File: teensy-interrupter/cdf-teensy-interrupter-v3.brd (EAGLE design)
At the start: 76.2 x 80 mm, 42 parts, among them IC1 TP4056, Q1 BC817-40LT1SMD

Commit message: More work
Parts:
- removed MIDI, PULSE: 100SP1T1B4M2QE, keves:100SP1T1B4M2QE
- removed PULSE_DUTY, PULSE_WIDTH: 10K PTV09A-4025F-B103, Bourns:PTV09A-4
- removed SW1: (no value), adafruit:EG1390
- added D1, D3: 1A/23V/620mV, SparkFun-DiscreteSemi:SOD-323
- added PWR: 100SP1T1B4M2QE, keves:100SP1T1B4M2QE
- added R12: 50000, rcl:R0805
- added R13: 100000, rcl:R0805
- added S1: ENCODER-2LED, SparkFun-Switches:ENCODER_LED_2
- R3, R5: value 330 -> 100
- R7: value 68 -> 27
- moved R11 111.0 mm to (57.4, 17.5), turned to 180 degrees
- moved C1 103.7 mm to (57.3, 15.0), turned to 180 degrees
- moved VUSB 103.6 mm to (43.7, 2.67)
- moved CHARGED 101.5 mm to (75.6, 14.7), turned to 90 degrees
- moved CHARGING 95.8 mm to (75.9, 18.2), turned to 90 degrees
- moved R8 85.0 mm to (70.9, 14.6)
- moved R6 84.4 mm to (71.8, 17.9)
- moved B- 73.2 mm to (67.7, 2.41), turned to 90 degrees
- moved B+ 69.3 mm to (64.9, 2.41), turned to 90 degrees
- moved IC1 68.5 mm to (64.3, 16.4)
- moved U$4 58.8 mm to (0.76, 33.9), turned to 90 degrees
- moved FB2 34.2 mm to (19.6, 28.8), turned to 180 degrees
- moved R2 32.6 mm to (19.7, 42.4), turned to 0 degrees
- moved C3 32.6 mm to (19.7, 32.4), turned to 180 degrees
- moved FB1 31.9 mm to (19.7, 39.0), turned to 180 degrees
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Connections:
- net RX renamed MIDI_RX
- removed net PULSE_DUTY: PULSE_DUTY.2, U$1.15/A1
- removed net PULSE_WIDTH: PULSE_WIDTH.2, U$1.14/A0
- removed net TX2: U$1.22/A8
- removed net TX3: U$1.23/A9
- new net ENC_A: S1.A, U$1.14/A0
- new net ENC_B: S1.B, U$1.15/A1
- new net ENC_Z: S1.SW, U$1.16/A2
- new net N$23: B+.1, D3.A, IC1.5
- new net V_SENSE: R12.1, R13.2
- net +3V3: now also R5.2, S1.C, U$3.2; no longer MIDI.P$1, PULSE.P$1, PULSE_DUTY.3, PULSE_WIDTH.3
- net +5V: now also VR1.1; no longer R3.2, R5.2, R7.2, U$3.2, VR1.3
- net GND: now also R13.1, VR1.3; no longer MIDI.P$3, PULSE.P$3, PULSE_DUTY.1, PULSE_WIDTH.1, VR1.1
- net MIDI_MODE: no longer MIDI.P$2
- net N$20: now also D1.C, D3.C, PWR.P$2; no longer B+.1, IC1.5, SW1.O2, SW1.S1
- net N$22: now also D1.A, VUSB.1; no longer SW1.P1
- net N$24: now also R3.2, R7.2; no longer SW1.O1, SW1.S2, VUSB.1
- net PULSE_MODE: no longer PULSE.P$2
- net V+: now also PWR.P$3, R12.2; no longer SW1.P2
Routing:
- net +3V3: track 56.6 -> 0.00 mm
- net MIDI_MODE: track 38.9 -> 0.00 mm, vias 1 -> 0
- net PULSE_MODE: track 35.6 -> 0.00 mm, vias 1 -> 0
- net PULSE_DUTY: track 29.0 -> 0.00 mm
- net PULSE_WIDTH: track 15.3 -> 0.00 mm
- net EMERGENCY: track 49.3 -> 55.8 mm

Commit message: WIP?
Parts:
- removed B+, B-: (no value), adafruit:1X01
- removed EMERGENCY: TL1105LF250Q, SparkFun-Electromechanical:TACTILE-PTH
- removed R4: 220, rcl:0204/7
- removed U$1: TEENSY_3.1_DIL, Teensy_3_and_LC_Series_Boards_v1.1:TEENSY3-DIL
- removed U$3: LCD-HD447804-HOLES16X2-4-HOLES, HD44780LCD:LCD-16X2-4HOLES
- removed U$4: MIDIJACK, adafruit:CP-2350
- removed VR1: 10k, SparkFun-Resistors:TRIMPOT-PTH-3386U
- added BATT, ESTOP: (no value), pinhead:1X02
- added MIDI: MIDIJACK, adafruit:CP-2350
- added R14, R15: 100, rcl:R0805
- added SCRN: (no value), adafruit:1X03
- added TEENSY: TEENSY_3.1_DIL, Teensy_3_and_LC_Series_Boards_v1.1:TEENSY3-DIL
- moved S1 95.0 mm to (61.2, 67.3), turned to 270 degrees
- moved H3 89.8 mm to (90.2, 57.7)
- moved OPT1 76.9 mm to (42.0, 2.16), turned to 180 degrees
- moved R12 76.5 mm to (39.6, 40.1)
- moved R13 74.1 mm to (39.6, 42.7)
- moved LED_TX 69.0 mm to (47.8, 5.71), turned to 180 degrees
- moved R3 56.7 mm to (44.6, 14.9), turned to 180 degrees
- moved R7 56.2 mm to (40.0, 14.9)
- moved C3 47.0 mm to (60.1, 8.38), flipped to the top, turned to 90 degrees
- moved Q1 46.7 mm to (45.0, 18.9), turned to 270 degrees
- moved FB2 46.3 mm to (65.2, 20.8), flipped to the top, turned to 90 degrees
- moved LED_POWER 44.2 mm to (45.7, 67.3)
- moved C2 43.2 mm to (60.1, 20.6), flipped to the top, turned to 90 degrees
- moved R5 43.1 mm to (49.8, 67.3)
- moved FB1 39.8 mm to (55.0, 20.7), flipped to the top, turned to 90 degrees
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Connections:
- removed net +5V: R4.1, VR1.1
- removed net LCD_D4: U$1.5, U$3.11
- removed net LCD_D5: U$1.6, U$3.12
- removed net LCD_D6: U$1.7, U$3.13
- removed net LCD_D7: U$1.8, U$3.14
- removed net LCD_EN: U$1.4, U$3.6
- removed net LCD_RS: U$1.3, U$3.4
- removed net MIDI_MODE: U$1.10
- removed net N$23: B+.1, D3.A, IC1.5
- removed net N$5: U$3.3, VR1.2
- removed net N$6: R4.2, U$3.15
- removed net PULSE_MODE: U$1.9
- new net B+: BATT.2, D3.A, IC1.5
- new net B+1: ESTOP.2
- new net IND_G: R15.1, TEENSY.17/A3
- new net IND_R: R14.1, TEENSY.18/A4
- new net N$25: R15.2, S1.+G
- new net N$26: R14.2, S1.+R
- new net SCRN_TX: SCRN.1, TEENSY.1
- net +3V3: now also SCRN.3, TEENSY.3.3V; no longer U$1.3.3V, U$3.2
- net AGND: now also TEENSY.AGND; no longer U$1.AGND
- net EMERGENCY: now also TEENSY.19/A5; no longer EMERGENCY.1, U$1.11
- net ENC_A: now also TEENSY.15/A1; no longer U$1.14/A0
- net ENC_B: now also TEENSY.14/A0; no longer U$1.15/A1
- net ENC_Z: now also TEENSY.16/A2; no longer U$1.16/A2
- net GND: now also BATT.1, ESTOP.1, SCRN.2, TEENSY.GND; no longer B-.1, EMERGENCY.3, U$1.GND, U$3.1, U$3.16, U$3.5, VR1.3
- net MIDI_RX: now also TEENSY.0; no longer U$1.0
- net N$1: now also MIDI.4; no longer U$4.4
- net N$13: now also MIDI.2; no longer U$4.2
- net N$14: now also MIDI.PE, MIDI.PE1, MIDI.PE2, MIDI.PE@; no longer U$4.PE, U$4.PE1, U$4.PE2, U$4.PE@
- net N$15: now also MIDI.5; no longer U$4.5
- net TX1: now also TEENSY.21/A7; no longer U$1.21/A7
- net V+: now also TEENSY.VIN; no longer U$1.VIN
- net V_SENSE: now also TEENSY.20/A6
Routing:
- net ENC_Z: track 0.00 -> 87.0 mm
- net MIDI_RX: track 0.00 -> 84.0 mm, vias 0 -> 1
- net ENC_A: track 0.00 -> 66.9 mm
- net ENC_B: track 0.00 -> 60.7 mm
- net EMERGENCY: track 55.8 -> 5.46 mm
- net N$26: track 0.00 -> 49.9 mm
- net V+: track 0.00 -> 48.6 mm
- net N$25: track 0.00 -> 42.1 mm
- net N$22: track 0.00 -> 38.3 mm
- net V_SENSE: track 0.00 -> 29.7 mm
- net IND_G: track 0.00 -> 29.5 mm
- net B+: track 0.00 -> 26.2 mm
- net LCD_D4: track 19.0 -> 0.00 mm
- net LCD_D5: track 18.6 -> 0.00 mm
- net LCD_D7: track 18.5 -> 0.00 mm
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- added copper zone on layer 1, net +3V3
- removed copper zone on layer 1, net +5V
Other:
- board size 76.2 x 80 mm -> 75.6 x 80.4 mm
- board text added: "CDF Interrupter v3 2021"
- board text removed: "CDF Interrupter v2 )'( 2017"

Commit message: v3 first press
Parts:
- removed D2: (no value), diode:DO-214AC
- removed LED_TX: (no value), adafruit:CHIP-LED0805
- removed PWR: 100SP1T1B4M2QE, keves:100SP1T1B4M2QE
- added D4: 1A/23V/620mV, SparkFun-DiscreteSemi:SOD-323
- added POWER: (no value), pinhead:1X02
- added TX1: (no value), adafruit:CHIP-LED0805
- H1, H2, H3, H4: value MOUNT-HOLE3.3 -> MOUNT-PAD-ROUND3.0; device holes:3,3 -> holes:3,0-PAD
- moved H3 101.8 mm to (3.81, 3.81), turned to 0 degrees
- moved H1 74.4 mm to (68.6, 3.81), turned to 0 degrees
- moved R5 63.6 mm to (23.7, 9.27), turned to 270 degrees
- moved LED_POWER 58.3 mm to (23.7, 13.3), turned to 0 degrees
- moved BATT 51.2 mm to (12.8, 29.8)
- moved H4 50.7 mm to (3.81, 41.9), turned to 0 degrees
- moved ESTOP 45.4 mm to (12.8, 23.4), turned to 270 degrees
- moved S1 43.1 mm to (40.8, 29.3), turned to 180 degrees
- moved H2 38.4 mm to (68.6, 41.9), turned to 0 degrees
- moved SCRN 33.8 mm to (12.8, 15.6)
- moved R12 33.1 mm to (27.7, 9.27), turned to 270 degrees
- moved R13 31.4 mm to (27.7, 13.6), turned to 270 degrees
- moved VUSB 29.6 mm to (12.8, 35.0), turned to 90 degrees
- moved R14 25.7 mm to (26.7, 22.2), turned to 180 degrees
- moved R15 25.6 mm to (26.7, 24.8), turned to 180 degrees
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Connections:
- net N$24 renamed 3.3V
- removed net B+1: ESTOP.2
- net EMERGENCY: now also ESTOP.2, TEENSY.5; no longer TEENSY.19/A5
- net ENC_A: now also TEENSY.13; no longer TEENSY.15/A1
- net GND: now also H1.B3,0, H2.B3,0, H3.B3,0, H4.B3,0
- net N$10: now also TX1.A; no longer LED_TX.A
- net N$11: now also TX1.C; no longer LED_TX.C
- net N$2: now also D4.C; no longer D2.C
- net N$20: now also POWER.1; no longer PWR.P$2
- net N$3: now also D4.A; no longer D2.A
- net V+: now also POWER.2; no longer PWR.P$3
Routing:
- net ENC_Z: track 87.0 -> 13.7 mm
- net ENC_A: track 66.9 -> 13.1 mm
- net ENC_B: track 60.7 -> 8.58 mm
- net N$26: track 49.9 -> 17.5 mm
- net N$20: track 9.54 -> 41.5 mm
- net N$25: track 42.1 -> 15.6 mm
- net IND_G: track 29.5 -> 4.51 mm
- net V_SENSE: track 29.7 -> 9.16 mm
- net MIDI_RX: track 84.0 -> 64.1 mm, vias 1 -> 0
- net V+: track 48.6 -> 30.7 mm
- net IND_R: track 13.9 -> 4.51 mm
- net SCRN_TX: track 0.00 -> 7.77 mm
- net GND: track 13.9 -> 20.4 mm, vias 8 -> 9
- net N$10: track 9.02 -> 3.72 mm
- net N$3: track 14.3 -> 9.04 mm
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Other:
- board size 75.6 x 80.4 mm -> 72.4 x 45.7 mm
- board text added: "+"
- board text added: "-"

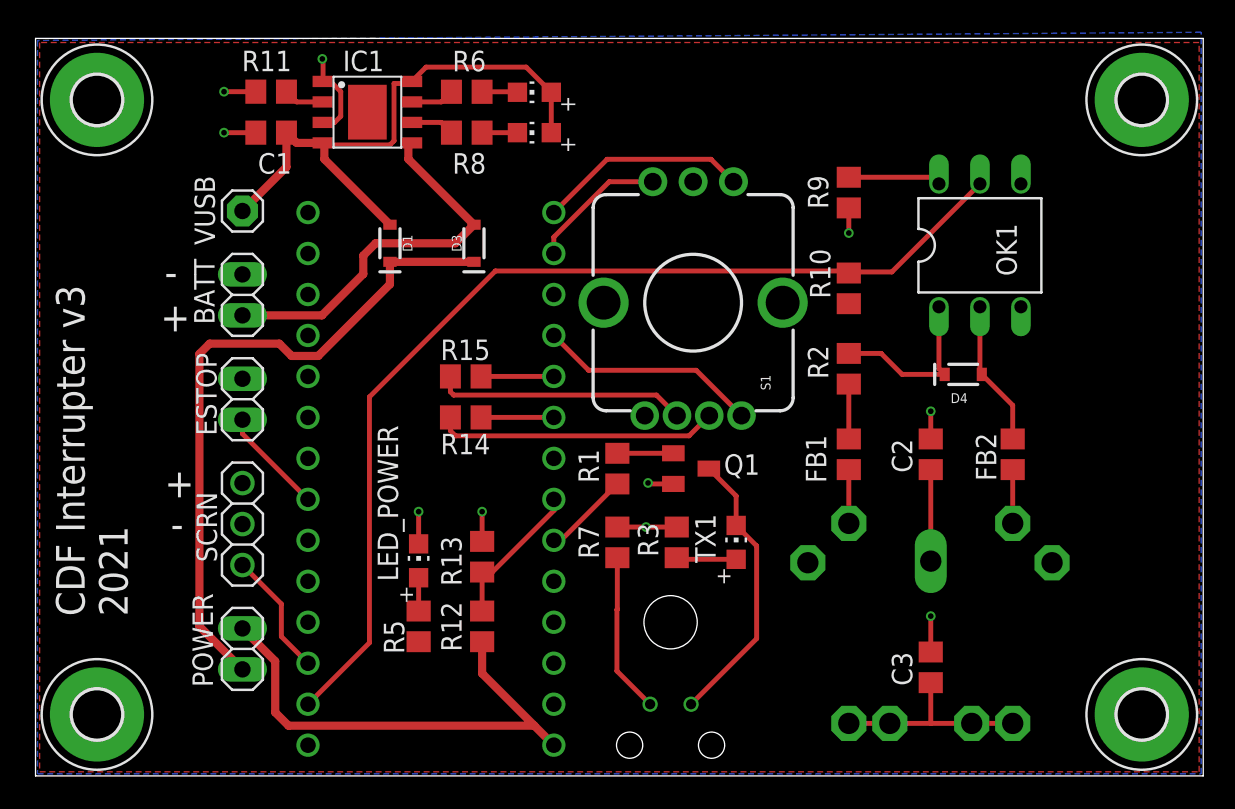
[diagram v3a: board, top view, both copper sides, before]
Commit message: Small board shrink
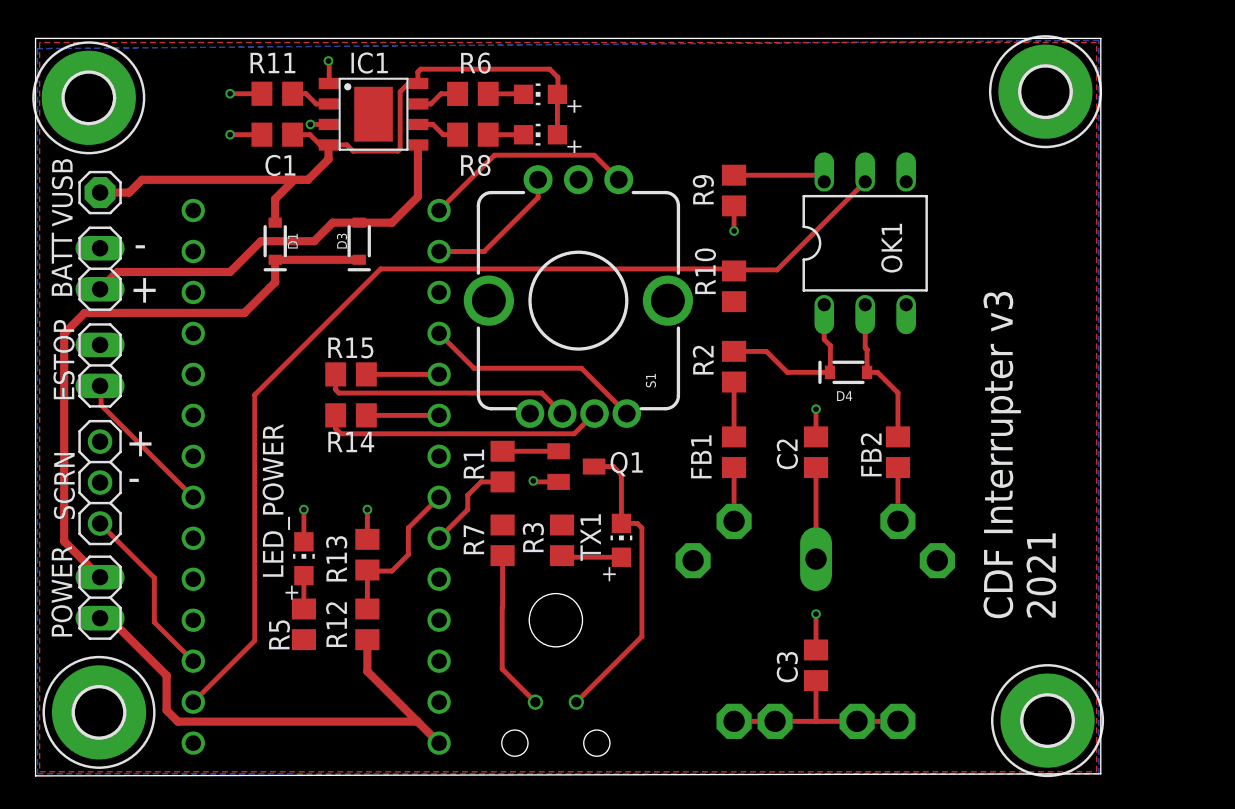
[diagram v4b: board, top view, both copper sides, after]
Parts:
- moved POWER 9.38 mm to (4.00, 11.0), turned to 270 degrees
- moved SCRN 9.19 mm to (4.00, 18.2)
- moved ESTOP 9.07 mm to (4.00, 25.4)
- moved BATT 8.97 mm to (4.00, 31.4)
- moved VUSB 8.90 mm to (4.00, 36.2)
- moved C2 7.11 mm to (48.4, 20.1)
- moved C3 7.11 mm to (48.4, 6.86)
- moved D3 7.11 mm to (20.1, 33.1)
- moved D4 7.11 mm to (50.4, 25.0)
- moved FB2 7.11 mm to (53.5, 20.1)
- moved MIDI 7.11 mm to (48.4, 0.76)
- moved Q1 7.11 mm to (33.5, 19.2)
- moved R14 7.11 mm to (19.6, 22.4)
- moved R15 7.11 mm to (19.6, 24.9)
- moved S1 7.11 mm to (33.7, 29.5)
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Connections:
- removed net 3.3V: R3.2, R7.2
- net +3V3: now also R3.2, R7.2
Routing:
- net N$22: track 36.7 -> 44.3 mm
- net N$20: track 41.5 -> 37.0 mm
- net 3.3V: track 3.68 -> 0.00 mm, vias 1 -> 0
- net SCRN_TX: track 7.77 -> 10.9 mm
- net EMERGENCY: track 6.62 -> 9.30 mm
- net GND: track 20.4 -> 17.9 mm, vias 9 -> 10
- net N$11: track 17.5 -> 18.8 mm
- net V+: track 30.7 -> 31.9 mm
- net B+: track 24.2 -> 25.3 mm
- net V_SENSE: track 9.16 -> 9.75 mm
- net TX1: track 5.38 -> 5.91 mm
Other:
- board size 72.4 x 45.7 mm -> 66 x 45.7 mm

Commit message: As printed
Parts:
- moved H3 0.72 mm to (3.43, 3.43)
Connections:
- net GND: now also S1.GND
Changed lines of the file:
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@@
 <attribute name="POPULARITY" value="17" x="62.611" y="42.418" size="1.778" layer="27" display="off"/>
 </element>
-<element name="H3" library="holes" library_urn="urn:adsk.eagle:library:237" package="3,0-PAD" package3d_urn="urn:adsk.eagle:package:14280/1" value="MOUNT-PAD-ROUND3.0" x="3.937" y="3.937" smashed="yes">
-<attribute name="POPULARITY" value="17" x="3.937" y="3.937" size="1.778" layer="27" display="off"/>
+<element name="H3" library="holes" library_urn="urn:adsk.eagle:library:237" package="3,0-PAD" package3d_urn="urn:adsk.eagle:package:14280/1" value="MOUNT-PAD-ROUND3.0" x="3.429" y="3.429" smashed="yes">
+<attribute name="POPULARITY" value="17" x="3.429" y="3.429" size="1.778" layer="27" display="off"/>
 </element>
 <element name="H4" library="holes" library_urn="urn:adsk.eagle:library:237" package="3,0-PAD" package3d_urn="urn:adsk.eagle:package:14280/1" value="MOUNT-PAD-ROUND3.0" x="3.302" y="42.037" smashed="yes">
@@
 <wire x1="51.435" y1="29.21" x2="51.435" y2="26.543" width="0.3048" layer="1"/>
 <wire x1="51.562" y1="26.416" x2="51.435" y2="26.543" width="0.3048" layer="1"/>
-<wire x1="51.562" y1="25.03095" x2="51.55005" y2="25.019" width="0.3048" layer="1"/>
+<wire x1="51.55005" y1="26.40405" x2="51.562" y2="26.416" width="0.3048" layer="1"/>
 <wire x1="51.55005" y1="25.019" x2="52.197" y2="25.019" width="0.3048" layer="1"/>
 <wire x1="51.55005" y1="25.019" x2="51.55005" y2="26.40405" width="0.3048" layer="1"/>
-<wire x1="51.55005" y1="26.40405" x2="51.562" y2="26.416" width="0.3048" layer="1"/>
 </signal>
 <signal name="GND" airwireshidden="yes">
@@
 <wire x1="18.205" y1="40.386" x2="17.0404" y2="40.386" width="0.3048" layer="1"/>
 <via x="17.0404" y="40.386" extent="1-16" drill="0.35"/>
+<contactref element="S1" pad="GND"/>
 </signal>
 <signal name="N$4">

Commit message: V3r1
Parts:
- removed R14, R15: 100, rcl:R0805
- removed S1: ENCODER-2LED, SparkFun-Switches:ENCODER_LED_2
- added C4: 10uF, rcl:C0805
- added J2, J3: 4p-2.54, OPL_Connector:H4-2.54
- added R16, R17: 100, rcl:R0805
- added R4: 10k, rcl:R0805
- R11: value 1.2K -> 10k
- moved BATT 26.8 mm to (30.6, 35.1), turned to 180 degrees
- moved CHARGING 25.9 mm to (20.8, 18.6), turned to 0 degrees
- moved CHARGED 25.3 mm to (17.7, 18.5), turned to 0 degrees
- moved VUSB 20.7 mm to (3.37, 15.5)
- moved R6 20.5 mm to (20.8, 22.8), turned to 270 degrees
- moved R8 19.5 mm to (17.7, 22.7), turned to 270 degrees
- moved D1 14.5 mm to (13.5, 18.7), turned to 270 degrees
- moved IC1 12.1 mm to (19.6, 29.0), turned to 270 degrees
- moved D3 11.1 mm to (13.5, 24.3)
- moved R11 10.3 mm to (21.8, 34.5)
- moved SCRN 9.24 mm to (3.49, 27.4), turned to 270 degrees
- moved D4 8.77 mm to (57.5, 19.9), turned to 90 degrees
- moved H2 7.64 mm to (62.1, 34.8)
- moved H4 7.27 mm to (3.94, 34.8)
- moved C1 5.54 mm to (16.9, 34.5), turned to 0 degrees
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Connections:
- net N$20 renamed SW
- net N$22 renamed V_USB
- removed net N$25: R15.2, S1.+G
- removed net N$26: R14.2, S1.+R
- new net N$20: J2.3, R16.1
- new net N$5: J3.1, R4.2
- new net N$6: J2.2, R17.1
- net +3V3: now also R4.1; no longer S1.C
- net B+: now also C4.1
- net ENC_A: now also J3.2; no longer S1.A
- net ENC_B: now also J3.3; no longer S1.B
- net ENC_Z: now also J2.1; no longer S1.SW
- net GND: now also C4.2, J2.4; no longer S1.GND
- net IND_G: now also R17.2; no longer R15.1
- net IND_R: now also R16.2; no longer R14.1
- net SCRN_TX: now also TEENSY.10; no longer TEENSY.1
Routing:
- net N$26: track 17.5 -> 0.00 mm
- net SW: track 37.0 -> 20.0 mm, vias 0 -> 1
- net N$25: track 15.6 -> 0.00 mm
- net N$2: track 10.8 -> 23.1 mm
- net ENC_B: track 8.63 -> 16.9 mm
- net B+: track 25.3 -> 33.1 mm
- net MIDI_RX: track 64.1 -> 58.9 mm
- net N$6: track 0.00 -> 4.70 mm
- net SCRN_TX: track 10.9 -> 6.30 mm
- net N$20: track 0.00 -> 4.30 mm
- net V_SENSE: track 9.75 -> 12.7 mm
- net N$5: track 0.00 -> 2.86 mm
- net ENC_A: track 13.2 -> 16.0 mm
- net GND: track 17.9 -> 20.6 mm, vias 10 -> 9
- net V+: track 31.9 -> 29.5 mm
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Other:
- board size 66 x 45.7 mm -> 66 x 38.1 mm

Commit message: WIP
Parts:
- removed LED_POWER: (no value), adafruit:CHIP-LED0805
- added PWR: (no value), adafruit:CHIP-LED0805
- moved VUSB 13.8 mm to (16.8, 12.6), turned to 270 degrees
- moved R5 3.86 mm to (13.3, 6.86)
- moved D3 3.06 mm to (13.2, 21.2)
- moved D1 1.92 mm to (13.2, 16.8)
- moved POWER 1.91 mm to (3.62, 12.6)
- moved R6 1.88 mm to (19.9, 21.1)
- moved C4 1.88 mm to (14.5, 27.3)
- moved CHARGED 1.88 mm to (16.8, 16.8)
- moved CHARGING 1.88 mm to (19.9, 17.0)
- moved IC1 1.88 mm to (18.7, 27.3)
- moved R8 1.88 mm to (16.8, 21.0)
- moved Q1 1.52 mm to (35.1, 19.2)
- moved R11 1.48 mm to (20.6, 33.8), turned to 90 degrees
- moved ESTOP 1.28 mm to (3.62, 19.1)
- moved R4 0.89 mm to (37.0, 35.4)
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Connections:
- net GND: now also PWR.C; no longer LED_POWER.C
- net N$9: now also PWR.A; no longer LED_POWER.A
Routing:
- net V_USB: track 43.1 -> 35.5 mm
- net SW: track 20.0 -> 15.3 mm, vias 1 -> 0
- net B+: track 33.1 -> 36.2 mm
- net V+: track 29.5 -> 26.7 mm
- net MIDI_RX: track 58.9 -> 61.2 mm
- net N$7: track 3.47 -> 5.00 mm
- net N$11: track 18.8 -> 17.5 mm
- net N$21: track 4.51 -> 3.45 mm
- net N$4: track 6.51 -> 5.54 mm
- net N$5: track 2.86 -> 3.75 mm
- net EMERGENCY: track 7.04 -> 6.39 mm
- net ENC_Z: track 11.5 -> 10.8 mm
- net GND: vias 9 -> 11
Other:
- outline, holes or cut-outs redrawn
